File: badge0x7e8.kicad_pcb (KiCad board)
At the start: 2 copper layers, 66 x 55 mm, 18 parts, among them Q1 Q_NPN_BEC, SW1 SW_SPDT

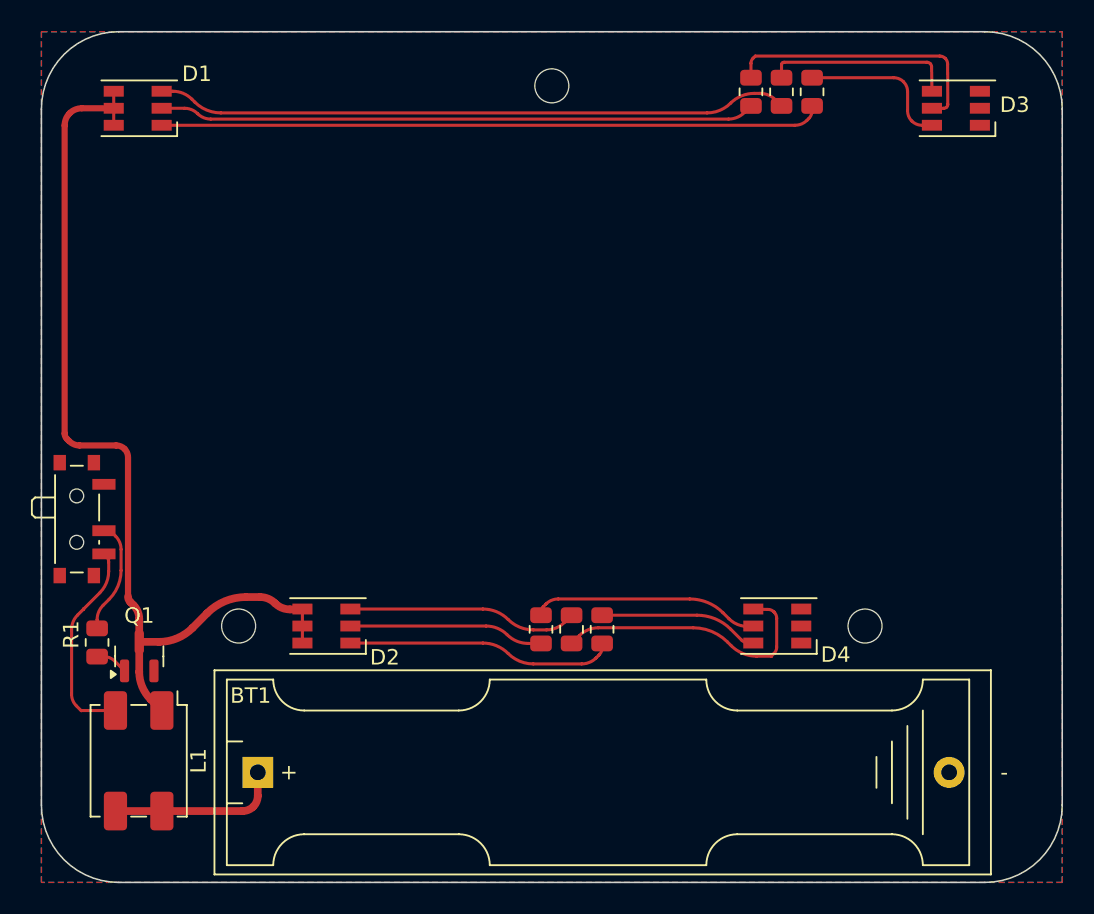
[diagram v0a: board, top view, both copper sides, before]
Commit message: Clearance adjustments
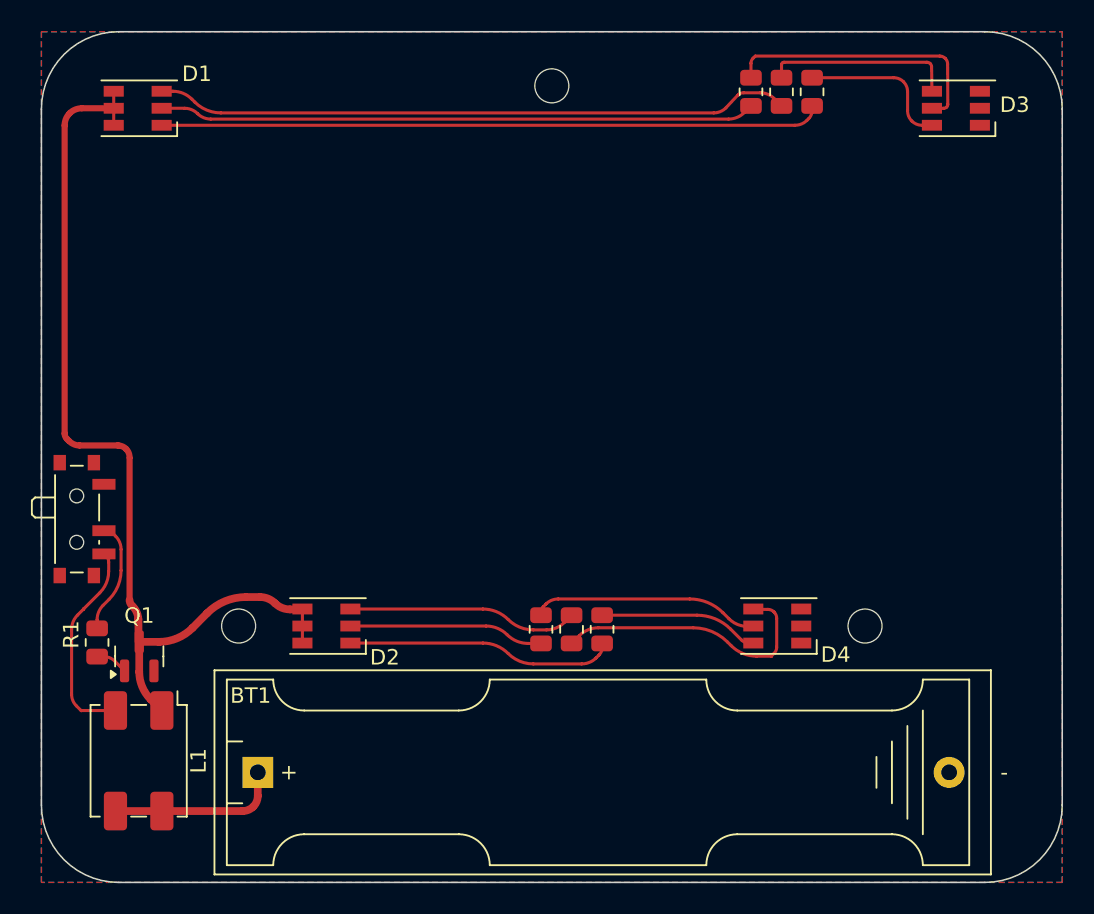
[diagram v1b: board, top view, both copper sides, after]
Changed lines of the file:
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@@
 	)
 	(segment
-		(start 146.462975 103.9875)
-		(end 146.082978 103.9875)
-		(width 0.2)
-		(layer "F.Cu")
-		(net 5)
-	)
-	(segment
-		(start 147.44375 104.39375)
+		(start 146.492222 103.95)
+		(end 145.403006 103.95)
+		(width 0.2)
+		(layer "F.Cu")
+		(net 5)
+	)
+	(segment
+		(start 144.251302 104.926463)
+		(end 145.025 104.1)
+		(width 0.2)
+		(layer "F.Cu")
+		(net 5)
+	)
+	(segment
+		(start 147.359053 104.309053)
 		(end 147.85 104.8)
 		(width 0.2)
@@
 	)
 	(segment
-		(start 109.915686 104.55)
-		(end 109.725045 104.359359)
+		(start 107.775 103.85)
+		(end 108.495343 103.85)
+		(width 0.2)
+		(layer "F.Cu")
+		(net 5)
+	)
+	(segment
+		(start 109.725045 104.359359)
+		(end 109.915686 104.55)
 		(width 0.2)
 		(layer "F.Cu")
@@
 	(segment
 		(start 111.605635 105.25)
-		(end 143.035033 105.25)
-		(width 0.2)
-		(layer "F.Cu")
-		(net 5)
-	)
-	(segment
-		(start 108.495343 103.85)
-		(end 107.775 103.85)
+		(end 143.47023 105.25)
+		(width 0.2)
+		(layer "F.Cu")
+		(net 5)
+	)
+	(arc
+		(start 143.47023 105.25)
+		(mid 143.892944 105.165915)
+		(end 144.251302 104.926463)
+		(width 0.2)
+		(layer "F.Cu")
+		(net 5)
+	)
+	(arc
+		(start 145.025 104.1)
+		(mid 145.191644 103.988649)
+		(end 145.388216 103.949548)
+		(width 0.2)
+		(layer "F.Cu")
+		(net 5)
+	)
+	(arc
+		(start 146.492222 103.95)
+		(mid 146.961347 104.043315)
+		(end 147.359053 104.309053)
 		(width 0.2)
 		(layer "F.Cu")
@@
 	)
 	(arc
-		(start 144.559006 104.61875)
-		(mid 145.25821 104.151556)
-		(end 146.082978 103.9875)
-		(width 0.2)
-		(layer "F.Cu")
-		(net 5)
-	)
-	(arc
-		(start 146.462975 103.9875)
-		(mid 146.993766 104.09308)
-		(end 147.44375 104.39375)
-		(width 0.2)
-		(layer "F.Cu")
-		(net 5)
-	)
-	(arc
-		(start 144.559006 104.61875)
-		(mid 143.859801 105.085943)
-		(end 143.035033 105.25)
-		(width 0.2)
-		(layer "F.Cu")
-		(net 5)
-	)
-	(arc
 		(start 109.915686 104.55)
 		(mid 110.691041 105.068075)
@@
 	)
 	(segment
-		(start 105.6 135.290625)
-		(end 105.6 127.518198)
+		(start 104.981801 126.75)
+		(end 102.463908 126.75)
 		(width 0.4)
 		(layer "F.Cu")
@@
 	)
 	(segment
-		(start 105.6 136.034375)
-		(end 105.6 136.40625)
-		(width 0.4)
-		(layer "F.Cu")
-		(net 6)
-	)
-	(segment
-		(start 102.463908 126.75)
-		(end 104.831801 126.75)
-		(width 0.4)
-		(layer "F.Cu")
-		(net 6)
-	)
-	(segment
 		(start 106.325 141.389789)
 		(end 106.325 139.45)
@@
 	)
 	(segment
-		(start 105.6 135.290625)
-		(end 105.6 136.034375)
-		(width 0.4)
-		(layer "F.Cu")
-		(net 6)
-	)
-	(segment
-		(start 106.325 137.962652)
-		(end 106.325 139.45)
+		(start 106.275 137.956323)
+		(end 106.275 139.443676)
 		(width 0.5)
 		(layer "F.Cu")
@@
 	)
 	(segment
+		(start 105.7 136.662876)
+		(end 105.7 127.575)
+		(width 0.4)
+		(layer "F.Cu")
+		(net 6)
+	)
+	(segment
 		(start 101.638866 126.313866)
 		(end 101.777162 126.452162)
-		(width 0.4)
-		(layer "F.Cu")
-		(net 6)
-	)
-	(segment
-		(start 105.9625 137.0875)
-		(end 105.75026 136.87526)
-		(width 0.5)
-		(layer "F.Cu")
-		(net 6)
-	)
-	(arc
-		(start 105.375 126.975)
-		(mid 105.125778 126.808475)
-		(end 104.831801 126.75)
 		(width 0.4)
 		(layer "F.Cu")
@@
 	)
 	(arc
-		(start 106.325 137.962652)
-		(mid 106.230789 137.489023)
-		(end 105.9625 137.0875)
+		(start 106.2625 138.025147)
+		(mid 106.168291 137.551524)
+		(end 105.9 137.15)
 		(width 0.5)
 		(layer "F.Cu")
@@
 	)
 	(arc
-		(start 105.375 126.975)
-		(mid 105.541524 127.224221)
-		(end 105.6 127.518198)
+		(start 105.475 126.975)
+		(mid 105.225778 126.808475)
+		(end 104.931801 126.75)
+		(width 0.4)
+		(layer "F.Cu")
+		(net 6)
+	)
+	(arc
+		(start 102.463908 126.75)
+		(mid 102.104603 126.678529)
+		(end 101.8 126.475)
 		(width 0.4)
 		(layer "F.Cu")
@@
 	)
 	(arc
-		(start 102.463908 126.75)
-		(mid 102.104603 126.678529)
-		(end 101.8 126.475)
-		(width 0.4)
-		(layer "F.Cu")
-		(net 6)
-	)
-	(arc
 		(start 115.1 136.95)
 		(mid 114.656939 136.653956)
@@
 	)
 	(arc
+		(start 105.7 127.518198)
+		(mid 105.641524 127.224221)
+		(end 105.475 126.975)
+		(width 0.4)
+		(layer "F.Cu")
+		(net 6)
+	)
+	(arc
 		(start 110.711541 137.597487)
 		(mid 111.863502 136.82235)
@@
 	)
 	(arc
-		(start 105.75026 136.87526)
-		(mid 105.639051 136.708824)
-		(end 105.6 136.5125)
-		(width 0.5)
-		(layer "F.Cu")
+		(start 105.85 137.1)
+		(mid 105.738982 136.933853)
+		(end 105.7 136.737876)
+		(width 0.5)
+		(layer "F.Cu")

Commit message: Some silkscreen thingies
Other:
- board text added: "="
- board text added: "Camp++"

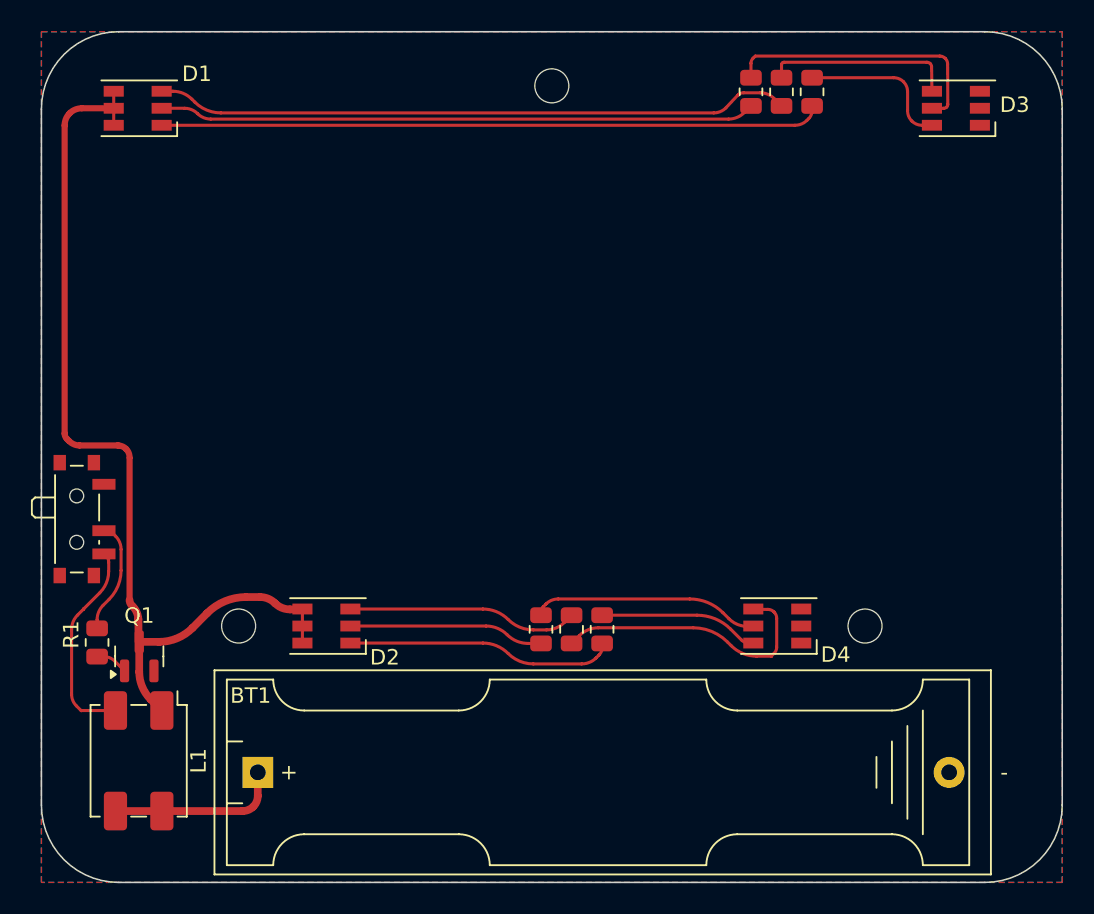
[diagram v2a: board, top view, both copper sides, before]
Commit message: Fix LED footprint, make others a bit more handsoler friendly
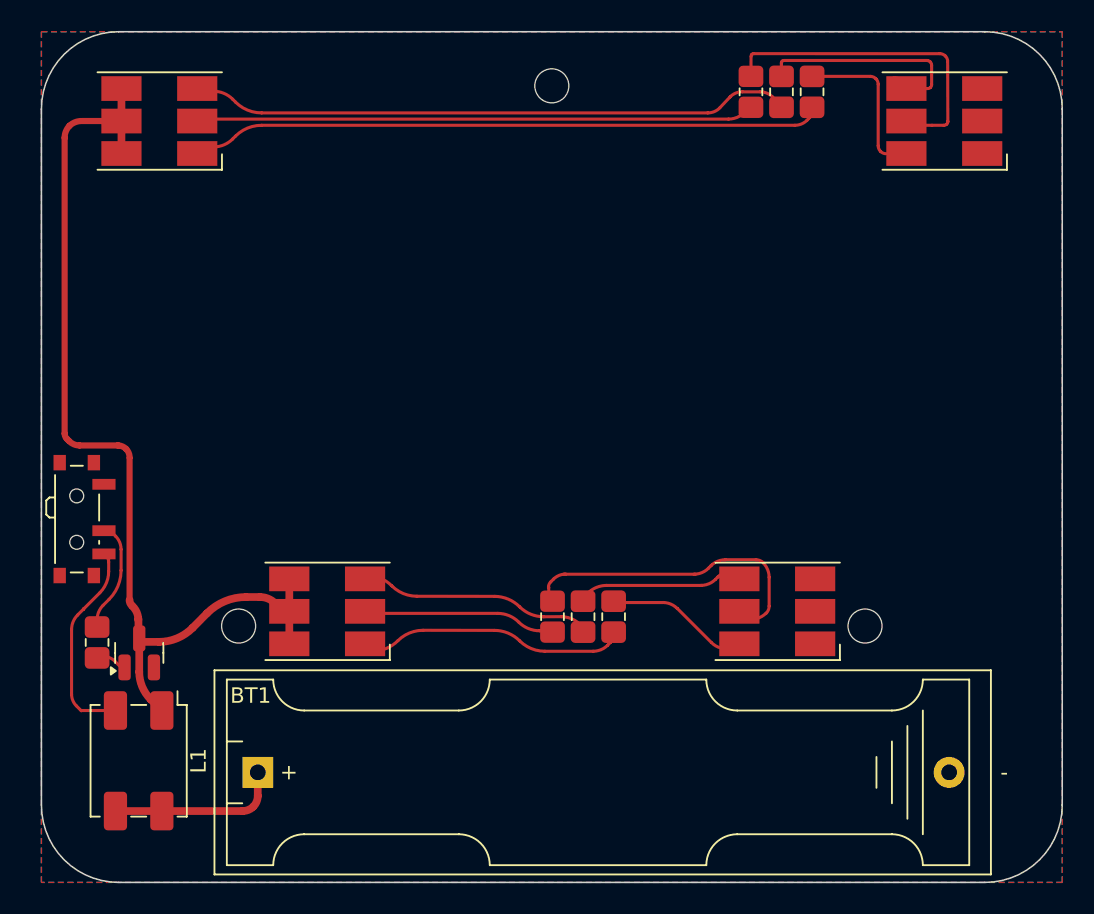
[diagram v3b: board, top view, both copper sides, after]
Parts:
- D1, D2, D3, D4: footprint LED_SMD:LED_RGB_PLCC-6 -> LED_SMD:LED_RGB_Cree-PLCC-6_6x5mm_P2.1mm
- R1, R2, R3, R4, R5, R6, R7: footprint Resistor_SMD:R_0805_2012Metric -> Resistor_SMD:R_0805_2012Metric_Pad1.20x1.40mm_HandSolder
- moved D1 1.63 mm to (107.6, 105.8)
- moved D3 1.11 mm to (158.4, 105.8)
- moved R5 1.11 mm to (137.0, 137.8)
- moved R7 1.11 mm to (135.0, 137.8), turned to 90 degrees
- moved R6 1.11 mm to (133.0, 137.8)
- moved D2 0.95 mm to (118.5, 137.5)
- moved D4 0.95 mm to (147.6, 137.5)
- moved Q1 0.22 mm to (106.3, 140.2)
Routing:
- net Net-(D4-AR): track 17.8 -> 10.5 mm
- net Net-(D4-AG): track 15.2 -> 20.5 mm
- net Net-(D1-KR): track 41.2 -> 37.6 mm
- net Net-(D3-AG): track 18.0 -> 21.6 mm
- net Net-(D1-KG): track 38.6 -> 35.2 mm
- net Net-(D1-AB): track 61.7 -> 64.9 mm
- net Net-(D3-AR): track 12.4 -> 14.7 mm
- net Net-(D1-KB): track 42.8 -> 40.6 mm
- net Net-(D4-AB): track 10.3 -> 8.34 mm
